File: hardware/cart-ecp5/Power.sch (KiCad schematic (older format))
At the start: 48 parts, among them U13 TLV62568DBV, U5 TPS2111A, U6 TLV62568DBV, U7 TLV62568DBV, U8 TLV73325PDBV

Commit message: Enlarge test points to 1mm diameter
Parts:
- TP10, TP11, TP12, TP13, TP2, TP3, TP4, TP5, TP6, TP7, TP8, TP9: footprint ng_test:TestPoint_Pad_D0.5mm -> TestPoint:TestPoint_Pad_D1.0mm
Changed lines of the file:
@@
 F 0 "TP6" H 9908 1418 50  0000 L CNN
 F 1 "TestPoint" H 9908 1327 50  0001 L CNN
-F 2 "ng_test:TestPoint_Pad_D0.5mm" H 10050 1300 50  0001 C CNN
+F 2 "TestPoint:TestPoint_Pad_D1.0mm" H 10050 1300 50  0001 C CNN
 F 3 "~" H 10050 1300 50  0001 C CNN
 	1    9850 1300
@@
 F 0 "TP9" H 9908 3218 50  0000 L CNN
 F 1 "TestPoint" H 9908 3127 50  0001 L CNN
-F 2 "ng_test:TestPoint_Pad_D0.5mm" H 10050 3100 50  0001 C CNN
+F 2 "TestPoint:TestPoint_Pad_D1.0mm" H 10050 3100 50  0001 C CNN
 F 3 "~" H 10050 3100 50  0001 C CNN
 	1    9850 3100
@@
 F 0 "TP12" H 9908 5018 50  0000 L CNN
 F 1 "TestPoint" H 9908 4927 50  0001 L CNN
-F 2 "ng_test:TestPoint_Pad_D0.5mm" H 10050 4900 50  0001 C CNN
+F 2 "TestPoint:TestPoint_Pad_D1.0mm" H 10050 4900 50  0001 C CNN
 F 3 "~" H 10050 4900 50  0001 C CNN
 	1    9850 4900
@@
 F 0 "TP3" H 1708 1418 50  0000 L CNN
 F 1 "TestPoint" H 1708 1327 50  0001 L CNN
-F 2 "ng_test:TestPoint_Pad_D0.5mm" H 1850 1300 50  0001 C CNN
+F 2 "TestPoint:TestPoint_Pad_D1.0mm" H 1850 1300 50  0001 C CNN
 F 3 "~" H 1850 1300 50  0001 C CNN
 	1    1650 1300
@@
 F 0 "TP10" H 4158 3468 50  0000 L CNN
 F 1 "TestPoint" H 4158 3377 50  0001 L CNN
-F 2 "ng_test:TestPoint_Pad_D0.5mm" H 4300 3350 50  0001 C CNN
+F 2 "TestPoint:TestPoint_Pad_D1.0mm" H 4300 3350 50  0001 C CNN
 F 3 "~" H 4300 3350 50  0001 C CNN
 	1    4100 3350
@@
 F 0 "TP5" H 6308 1418 50  0000 L CNN
 F 1 "TestPoint" H 6308 1327 50  0001 L CNN
-F 2 "ng_test:TestPoint_Pad_D0.5mm" H 6450 1300 50  0001 C CNN
+F 2 "TestPoint:TestPoint_Pad_D1.0mm" H 6450 1300 50  0001 C CNN
 F 3 "~" H 6450 1300 50  0001 C CNN
 	1    6250 1300
@@
 F 0 "TP2" H 1442 1418 50  0000 R CNN
 F 1 "TestPoint" H 1442 1327 50  0001 R CNN
-F 2 "ng_test:TestPoint_Pad_D0.5mm" H 1700 1300 50  0001 C CNN
+F 2 "TestPoint:TestPoint_Pad_D1.0mm" H 1700 1300 50  0001 C CNN
 F 3 "~" H 1700 1300 50  0001 C CNN
 	1    1500 1300
@@
 F 0 "TP4" H 4908 1418 50  0000 L CNN
 F 1 "TestPoint" H 4908 1327 50  0001 L CNN
-F 2 "ng_test:TestPoint_Pad_D0.5mm" H 5050 1300 50  0001 C CNN
+F 2 "TestPoint:TestPoint_Pad_D1.0mm" H 5050 1300 50  0001 C CNN
 F 3 "~" H 5050 1300 50  0001 C CNN
 	1    4850 1300
@@
 F 0 "TP7" H 3458 2018 50  0000 L CNN
 F 1 "TestPoint" H 3458 1927 50  0001 L CNN
-F 2 "ng_test:TestPoint_Pad_D0.5mm" H 3600 1900 50  0001 C CNN
+F 2 "TestPoint:TestPoint_Pad_D1.0mm" H 3600 1900 50  0001 C CNN
 F 3 "~" H 3600 1900 50  0001 C CNN
 	1    3400 1900
@@
 F 0 "TP8" V 8100 1900 50  0000 C CNN
 F 1 "TestPoint" V 8154 1972 50  0001 C CNN
-F 2 "ng_test:TestPoint_Pad_D0.5mm" H 8250 1900 50  0001 C CNN
+F 2 "TestPoint:TestPoint_Pad_D1.0mm" H 8250 1900 50  0001 C CNN
 F 3 "~" H 8250 1900 50  0001 C CNN
 	1    8050 1900
@@
 F 0 "TP11" V 8100 3700 50  0000 C CNN
 F 1 "TestPoint" V 8154 3772 50  0001 C CNN
-F 2 "ng_test:TestPoint_Pad_D0.5mm" H 8250 3700 50  0001 C CNN
+F 2 "TestPoint:TestPoint_Pad_D1.0mm" H 8250 3700 50  0001 C CNN
 F 3 "~" H 8250 3700 50  0001 C CNN
 	1    8050 3700
@@
 F 0 "TP13" V 8100 5500 50  0000 C CNN
 F 1 "TestPoint" V 8154 5572 50  0001 C CNN
-F 2 "ng_test:TestPoint_Pad_D0.5mm" H 8250 5500 50  0001 C CNN
+F 2 "TestPoint:TestPoint_Pad_D1.0mm" H 8250 5500 50  0001 C CNN
 F 3 "~" H 8250 5500 50  0001 C CNN
 	1    8050 5500

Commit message: Add header for injecting 3V3 rail without populating USB_3V3 regulator and power mux
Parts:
- added J4: Conn_01x02, Connector_PinHeader_2.54mm:PinHeader_1x02_P2.54mm_Vertical, symbol Connector_Generic:Conn_01x02
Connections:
- net GND: now also J4.1 (Pin_1)
- net P3V3: now also J4.2 (Pin_2)
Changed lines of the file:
@@
 	8200 5500 8050 5500
 Connection ~ 8200 5500
+$Comp
+L Connector_Generic:Conn_01x02 J4
+U 1 1 5FF61CAC
+P 3000 5550
+F 0 "J4" H 2950 5200 50  0000 C CNN
+F 1 "Conn_01x02" H 2950 5300 50  0000 C CNN
+F 2 "Connector_PinHeader_2.54mm:PinHeader_1x02_P2.54mm_Vertical" H 3000 5550 50  0001 C CNN
+F 3 "~" H 3000 5550 50  0001 C CNN
+	1    3000 5550
+	-1   0    0    1
+$EndComp
+Text GLabel 3400 5450 2    50   UnSpc ~ 0
+P3V3
+Wire Wire Line
+	3200 5450 3400 5450
+Wire Wire Line
+	3200 5550 3300 5550
+Wire Wire Line
+	3300 5550 3300 5650
+$Comp
+L ng_power:GND #PWR0102
+U 1 1 5FF79703
+P 3300 5650
+F 0 "#PWR0102" H 3300 5400 50  0001 C CNN
+F 1 "GND" H 3303 5524 50  0000 C CNN
+F 2 "" H 3200 5300 50  0001 C CNN
+F 3 "" H 3300 5650 50  0001 C CNN
+	1    3300 5650
+	1    0    0    -1
+$EndComp
 $EndSCHEMATC

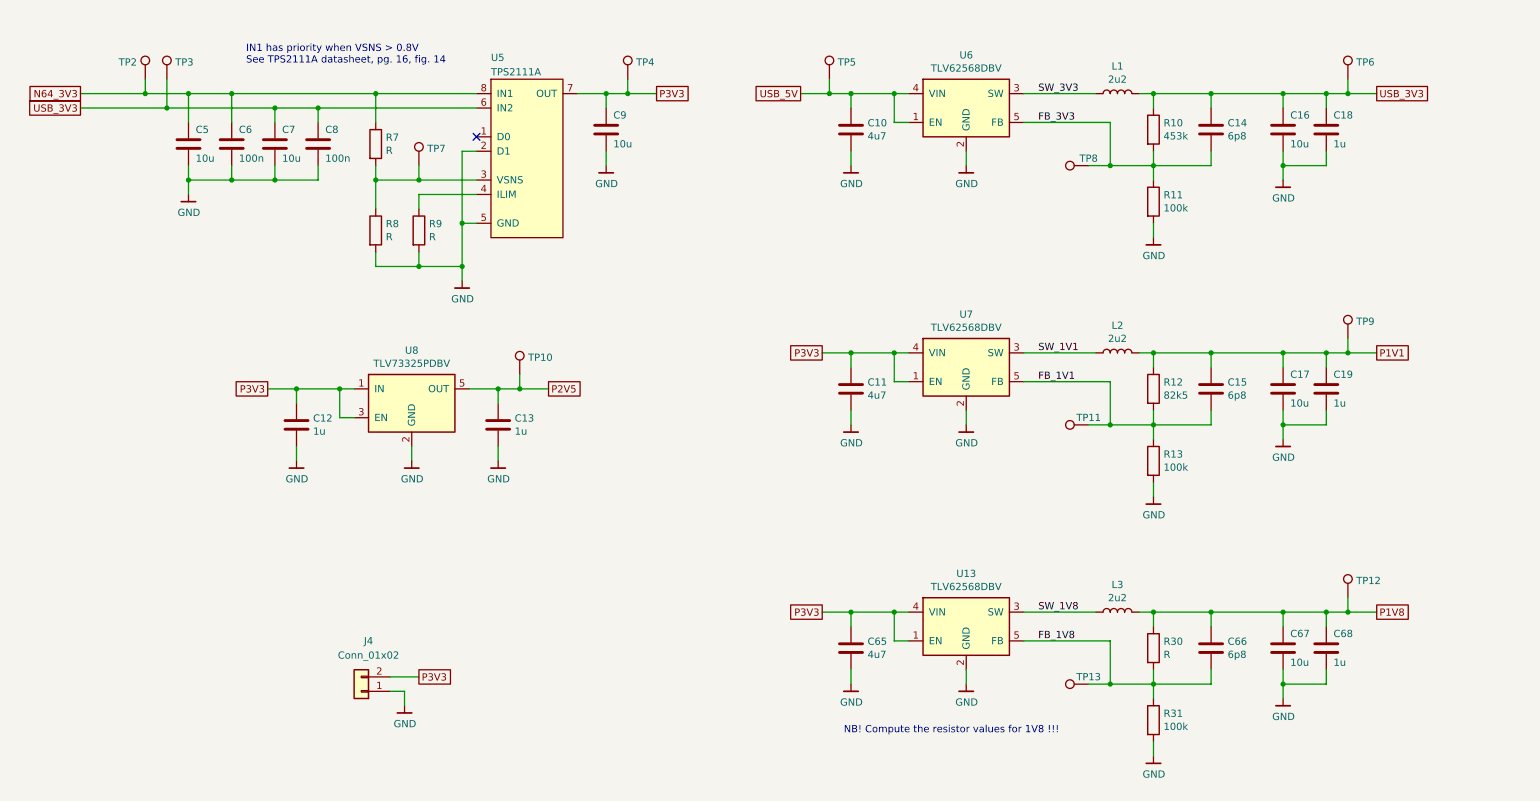
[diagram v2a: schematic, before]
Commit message: Check all resistor values for power management and assign MPN for caps and resistors
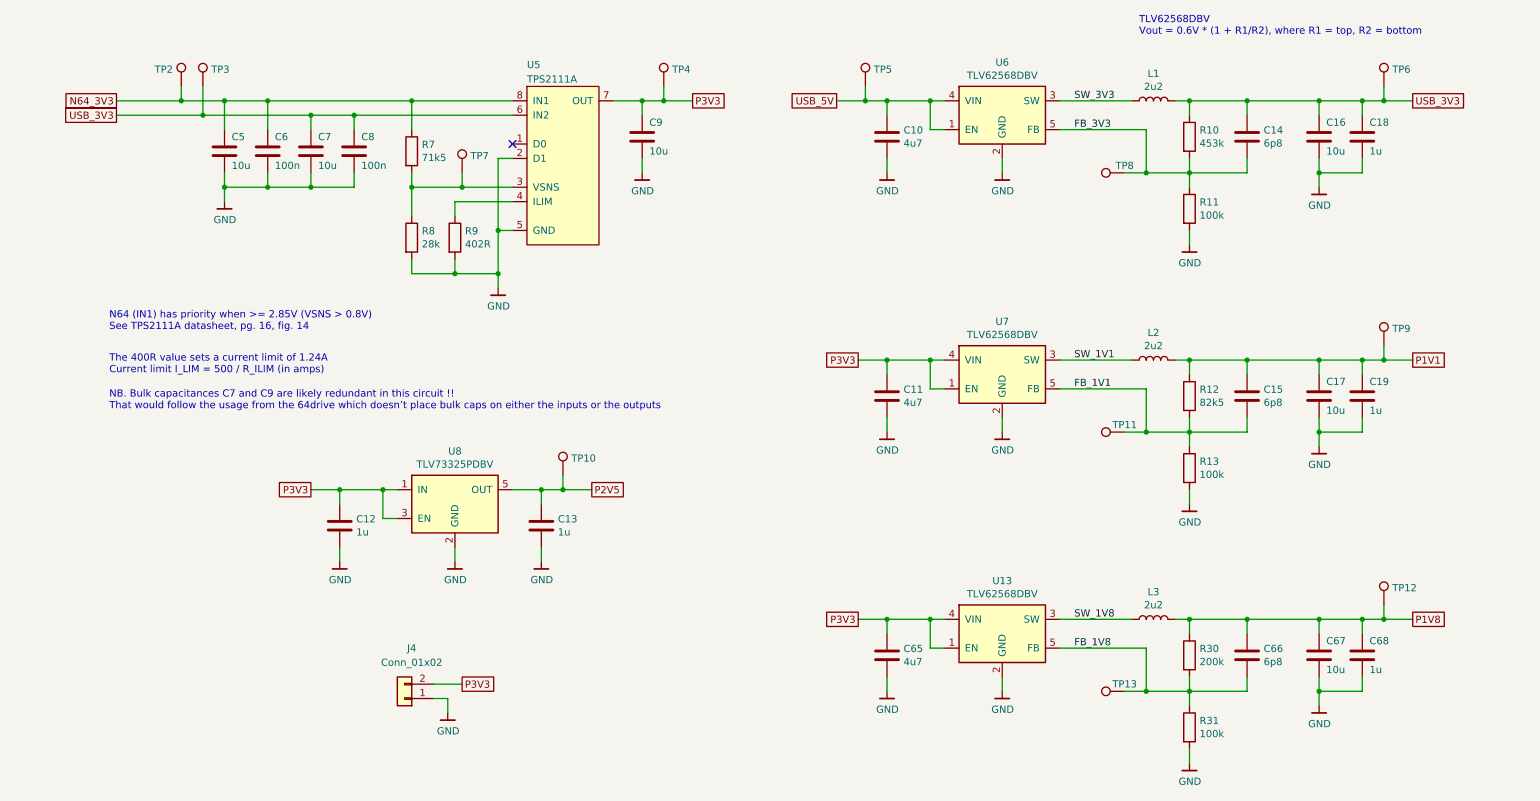
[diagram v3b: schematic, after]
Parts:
- C10, C11, C65: MFR (none) -> Samsung; MPN (none) -> CL05A475KP5NRNC
- C12, C13, C18, C19, C68: MFR (none) -> Samsung; MPN (none) -> CL05A105KO5NNNC
- C14, C15, C66: MFR (none) -> Yageo; MPN (none) -> CC0402CRNPO9BN6R8
- C16, C17, C3, C4, C51, C67: MFR (none) -> Samsung; MPN (none) -> CL10A106MQ8NNND
- C52, C53: MFR (none) -> Samsung; MPN (none) -> CL05B104KO5NNNC
- L1, L2, L3: MFR (none) -> Murata; MPN (none) -> LQM21PN2R2NGCD
- R10: MFR (none) -> Yageo; MPN (none) -> RC0402FR-07453KL
- R11, R13, R31: MFR (none) -> Yageo; MPN (none) -> RC0402FR-07100KL
- R12: MFR (none) -> Yageo; MPN (none) -> RC0402FR-0782K5L
- R30: value R -> 200k; MFR (none) -> Yageo; MPN (none) -> RC0402FR-07200KL
- R7: value R -> 71k5; MFR (none) -> Yageo; MPN (none) -> RC0402FR-0771K5L
- R8: value R -> 28k; MFR (none) -> Yageo; MPN (none) -> RC0402FR-0728KL
- R9: value R -> 402R; MFR (none) -> Yageo; MPN (none) -> RC0402FR-07402RL
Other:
- note added: "N64 (IN1) has priority when >= 2.85V (VSNS > 0.8V)\nSee TPS2111A datasheet, pg. 16, fig. 14"
- note added: "NB. Bulk capacitances C7 and C9 are likely redundant in this circuit !!\nThat would follow the usage from the 64drive which doesn’t place bulk caps on either the inputs or the outputs"
- note added: "TLV62568DBV\nVout = 0.6V * (1 + R1/R2), where R1 = top, R2 = bottom"
- note added: "The 400R value sets a current limit of 1.24A\nCurrent limit I_LIM = 500 / R_ILIM (in amps)"
- note removed: "IN1 has priority when VSNS > 0.8V\nSee TPS2111A datasheet, pg. 16, fig. 14"
- note removed: "NB! Compute the resistor values for 1V8 !!!"
- moved on the sheet: C10, C11, C12, C13, C14, C15, C16, C17, C18, C19, C5, C6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

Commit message: Assign MPN for all other components except oscillators
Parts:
- J4: MFR (none) -> Molex; MPN (none) -> 22284020
- U13, U6, U7: MFR (none) -> TI; MPN (none) -> TLV62568DBVR
- U5: MFR (none) -> TI; MPN (none) -> TPS2111APWR
- U8: MFR (none) -> TI; MPN (none) -> TLV73325PDBVR
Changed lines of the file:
@@
 F 2 "Package_TO_SOT_SMD:SOT-23-5" H 7450 2850 50  0001 C CNN
 F 3 "https://www.ti.com/lit/ds/symlink/tlv62568.pdf" H 7450 3250 50  0001 C CNN
+F 4 "TI" H 7450 3300 50  0001 C CNN "MFR"
+F 5 "TLV62568DBVR" H 7450 3300 50  0001 C CNN "MPN"
 	1    7450 3300
 	1    0    0    -1
@@
 F 2 "Package_TO_SOT_SMD:SOT-23-5" H 7450 1050 50  0001 C CNN
 F 3 "https://www.ti.com/lit/ds/symlink/tlv62568.pdf" H 7450 1450 50  0001 C CNN
+F 4 "TI" H 7450 1500 50  0001 C CNN "MFR"
+F 5 "TLV62568DBVR" H 7450 1500 50  0001 C CNN "MPN"
 	1    7450 1500
 	1    0    0    -1
@@
 F 2 "Package_TO_SOT_SMD:SOT-23-5" H 3650 3750 50  0001 C CNN
 F 3 "https://www.ti.com/lit/ds/symlink/tlv733p.pdf" H 3650 4150 50  0001 C CNN
+F 4 "TI" H 3650 4200 50  0001 C CNN "MFR"
+F 5 "TLV73325PDBVR" H 3650 4200 50  0001 C CNN "MPN"
 	1    3650 4200
 	1    0    0    -1
@@
 F 2 "Package_SO:TSSOP-8_4.4x3mm_P0.65mm" H 4400 1300 50  0001 C CNN
 F 3 "https://www.ti.com/lit/ds/symlink/tps2111a.pdf" H 4650 1850 50  0001 C CNN
+F 4 "TI" H 4400 1900 50  0001 C CNN "MFR"
+F 5 "TPS2111APWR" H 4400 1900 50  0001 C CNN "MPN"
 	1    4400 1900
 	1    0    0    -1
@@
 F 2 "Package_TO_SOT_SMD:SOT-23-5" H 7450 4650 50  0001 C CNN
 F 3 "https://www.ti.com/lit/ds/symlink/tlv62568.pdf" H 7450 5050 50  0001 C CNN
+F 4 "TI" H 7450 5100 50  0001 C CNN "MFR"
+F 5 "TLV62568DBVR" H 7450 5100 50  0001 C CNN "MPN"
 	1    7450 5100
 	1    0    0    -1
@@
 F 2 "Connector_PinHeader_2.54mm:PinHeader_1x02_P2.54mm_Vertical" H 3300 5600 50  0001 C CNN
 F 3 "~" H 3300 5600 50  0001 C CNN
+F 4 "Molex" H 3300 5600 50  0001 C CNN "MFR"
+F 5 "22284020" H 3300 5600 50  0001 C CNN "MPN"
 	1    3300 5600
 	-1   0    0    1
